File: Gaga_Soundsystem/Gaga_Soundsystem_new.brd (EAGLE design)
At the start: 160 x 100 mm, 16 parts, among them IC1 TUSB2046VF, Q2 6MHZ

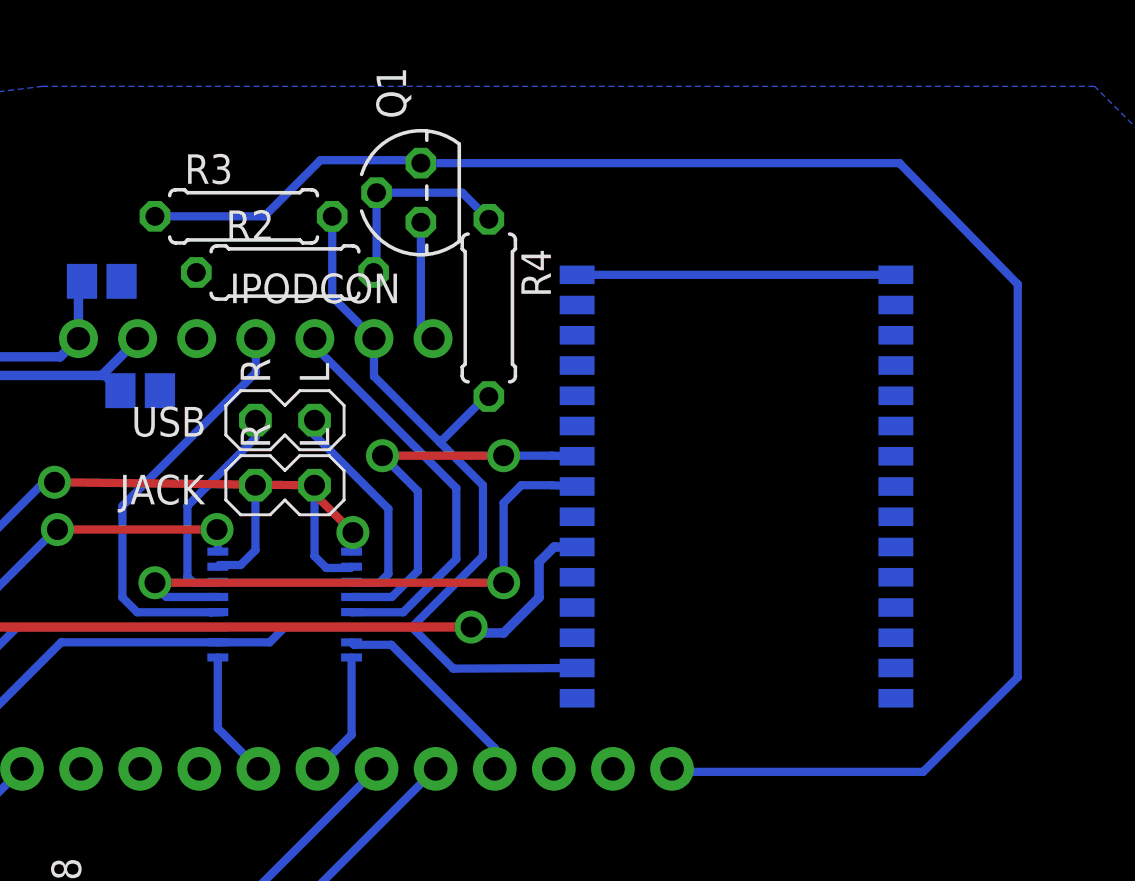
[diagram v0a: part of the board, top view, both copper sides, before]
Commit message: resistor to smd and add 3.3v
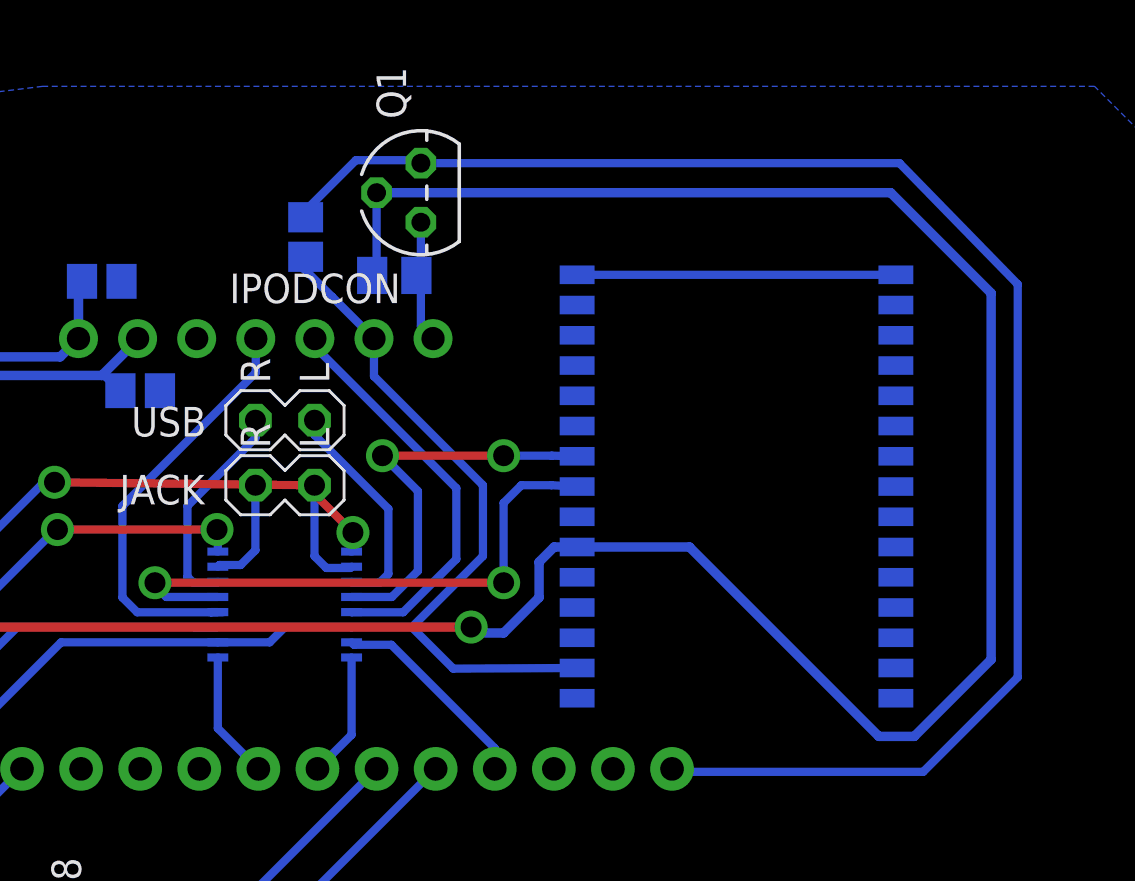
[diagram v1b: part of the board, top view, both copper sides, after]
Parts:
- removed R4: 4.7K, resistor:0207/7
- R2: device resistor:0207/7 -> resistor:M0805
- R3: device resistor:0207/7 -> resistor:R0805
- moved R2 4.70 mm to (101.1, 74.3), flipped to the bottom
- moved R3 2.81 mm to (97.3, 75.9), flipped to the bottom, turned to 270 degrees
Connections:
- removed net N$4: Q1.2, R2.2, R4.1
- net 3.3V: now also Q1.2, R2.2
- net 5.0V: no longer R4.2
- net GND: now also U$28.23, U$28.3; no longer R2.1
- net N$1: now also R2.1
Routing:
- net 3.3V: track 57.5 -> 127.7 mm
- net N$4: track 8.78 -> 0.00 mm
- net TX0: track 73.8 -> 67.9 mm
- net 5.0V: track 112.4 -> 109.0 mm
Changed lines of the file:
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@@
 <element name="U$28" library="SparkFun-Boards" package="ARDUINO_PRO_MICRO" value="ARDUINO_PRO_MICRO" x="100.33" y="45.466" rot="R270"/>
 <element name="Q1" library="transistors" package="TO-92" value="" x="102.235" y="77.851" rot="R90"/>
-<element name="R2" library="resistor" package="0207/7" value="10K" x="96.393" y="74.422"/>
-<element name="R3" library="resistor" package="0207/7" value="10K" x="94.615" y="76.835"/>
-<element name="R4" library="resistor" package="0207/7" value="4.7K" x="105.156" y="72.898" rot="R270"/>
+<element name="R2" library="resistor" package="M0805" value="10K" x="101.092" y="74.295" rot="MR0"/>
+<element name="R3" library="resistor" package="R0805" value="10K" x="97.282" y="75.946" rot="MR270"/>
 <element name="IC1" library="jt-texas" package="TQFP32-08" value="TUSB2046VF" x="78.74" y="69.596" rot="MR270"/>
 <element name="Q2" library="crystal" package="HC49/S" value="6MHZ" x="70.739" y="69.342" rot="R90">
@@
 <contactref element="Q1" pad="3"/>
 <contactref element="R3" pad="1"/>
-<wire x1="90.805" y1="76.835" x2="95.504" y2="76.835" width="0.3556" layer="16"/>
-<wire x1="95.504" y1="76.835" x2="97.917" y2="79.248" width="0.3556" layer="16"/>
-<wire x1="97.917" y1="79.248" x2="102.108" y2="79.248" width="0.3556" layer="16"/>
+<wire x1="97.028" y1="76.835" x2="97.282" y2="77.089" width="0.3556" layer="16"/>
+<wire x1="97.282" y1="77.089" x2="99.441" y2="79.248" width="0.3556" layer="16"/>
+<wire x1="99.441" y1="79.248" x2="102.108" y2="79.248" width="0.3556" layer="16"/>
 <wire x1="102.108" y1="79.248" x2="102.235" y2="79.121" width="0.3556" layer="16"/>
 <wire x1="102.235" y1="79.121" x2="122.809" y2="79.121" width="0.3556" layer="16"/>
@@
 <wire x1="123.825" y1="52.959" x2="113.157" y2="52.959" width="0.3556" layer="16"/>
 <wire x1="113.157" y1="52.959" x2="113.03" y2="53.086" width="0.3556" layer="16"/>
+<wire x1="97.282" y1="76.796" x2="97.282" y2="77.089" width="0.4064" layer="16"/>
 </signal>
 <signal name="GND">
@@
 <wire x1="93.506" y1="59.175" x2="84.881" y2="59.175" width="0.3556" layer="16"/>
 <wire x1="84.881" y1="59.175" x2="78.971" y2="53.265" width="0.3556" layer="16"/>
-<contactref element="R2" pad="1"/>
 <contactref element="IC1" pad="7"/>
 <contactref element="IC1" pad="28"/>
@@
 <wire x1="71.882" y1="65.405" x2="71.755" y2="62.865" width="0.4064" layer="16"/>
 <contactref element="IC1" pad="8"/>
+<contactref element="U$28" pad="3"/>
+<contactref element="U$28" pad="23"/>
+<wire x1="122.651" y1="56.122" x2="108.951" y2="56.122" width="0" layer="19" extent="16-16"/>
 </signal>
 <signal name="N$3">
@@
 <wire x1="101.847" y1="59.175" x2="104.902" y2="62.23" width="0.3556" layer="16"/>
 <wire x1="104.902" y1="62.23" x2="104.902" y2="65.278" width="0.3556" layer="16"/>
-<wire x1="104.902" y1="65.278" x2="103.0605" y2="67.1195" width="0.3556" layer="16"/>
-<wire x1="103.0605" y1="67.1195" x2="100.218" y2="69.962" width="0.3556" layer="16"/>
+<wire x1="104.902" y1="65.278" x2="100.218" y2="69.962" width="0.3556" layer="16"/>
 <wire x1="108.951" y1="57.422" x2="103.627" y2="57.395" width="0.3556" layer="16"/>
 <wire x1="103.627" y1="57.395" x2="101.847" y2="59.175" width="0.3556" layer="16"/>
@@
 <wire x1="76.151" y1="49.358" x2="73.914" y2="47.121" width="0.3556" layer="16"/>
 <contactref element="R3" pad="2"/>
-<contactref element="R4" pad="2"/>
-<wire x1="98.425" y1="76.835" x2="98.425" y2="73.373" width="0.3556" layer="16"/>
+<wire x1="96.735" y1="75.057" x2="97.199971875" y2="74.593678125" width="0.3556" layer="16"/>
+<wire x1="97.199971875" y1="74.593678125" x2="98.425" y2="73.373" width="0.3556" layer="16"/>
 <wire x1="98.425" y1="73.373" x2="100.218" y2="71.58" width="0.3556" layer="16"/>
-<wire x1="105.156" y1="69.088" x2="105.029" y2="69.088" width="0.3556" layer="16"/>
-<wire x1="105.029" y1="69.088" x2="103.0605" y2="67.1195" width="0.3556" layer="16"/>
+<wire x1="97.282" y1="75.096" x2="97.199971875" y2="75.096" width="0.4064" layer="16"/>
+<wire x1="97.199971875" y1="75.096" x2="97.199971875" y2="74.593678125" width="0.4064" layer="16"/>
 </signal>
 <signal name="IPODR">
@@
 <contactref element="Q1" pad="1"/>
 <contactref element="U$5" pad="P$5"/>
-<wire x1="102.235" y1="76.581" x2="102.235" y2="72.103" width="0.3556" layer="16"/>
+<wire x1="102.235" y1="76.581" x2="102.235" y2="74.422" width="0.3556" layer="16"/>
+<wire x1="102.235" y1="74.422" x2="102.235" y2="72.103" width="0.3556" layer="16"/>
 <wire x1="102.235" y1="72.103" x2="102.758" y2="71.58" width="0.3556" layer="16"/>
-</signal>
-<signal name="N$4">
-<contactref element="Q1" pad="2"/>
-<contactref element="R2" pad="2"/>
-<contactref element="R4" pad="1"/>
-<wire x1="100.33" y1="77.851" x2="104.013" y2="77.851" width="0.3556" layer="16"/>
-<wire x1="104.013" y1="77.851" x2="105.156" y2="76.708" width="0.3556" layer="16"/>
-<wire x1="100.33" y1="77.851" x2="100.33" y2="74.549" width="0.3556" layer="16"/>
-<wire x1="100.33" y1="74.549" x2="100.203" y2="74.422" width="0.3556" layer="16"/>
+<contactref element="R2" pad="1"/>
+<wire x1="102.042" y1="74.295" x2="102.235" y2="74.295" width="0.4064" layer="16"/>
+<wire x1="102.235" y1="74.295" x2="102.235" y2="74.422" width="0.4064" layer="16"/>
 </signal>
 <signal name="N$2">
@@
 <wire x1="79.94" y1="73.8886" x2="79.94" y2="72.701" width="0.4064" layer="16"/>
 <wire x1="79.94" y1="72.701" x2="77.47" y2="70.231" width="0.4064" layer="16"/>
+<contactref element="Q1" pad="2"/>
+<contactref element="R2" pad="2"/>
+<wire x1="100.33" y1="77.851" x2="100.33" y2="74.549" width="0.3556" layer="16"/>
+<wire x1="100.142" y1="74.295" x2="100.33" y2="74.295" width="0.4064" layer="16"/>
+<wire x1="100.33" y1="74.295" x2="100.33" y2="74.549" width="0.4064" layer="16"/>
+<wire x1="108.951" y1="62.622" x2="113.781" y2="62.622" width="0.4064" layer="16"/>
+<wire x1="113.781" y1="62.622" x2="121.92" y2="54.483" width="0.4064" layer="16"/>
+<wire x1="121.92" y1="54.483" x2="123.444" y2="54.483" width="0.4064" layer="16"/>
+<wire x1="123.444" y1="54.483" x2="126.746" y2="57.785" width="0.4064" layer="16"/>
+<wire x1="126.746" y1="57.785" x2="126.746" y2="73.533" width="0.4064" layer="16"/>
+<wire x1="126.746" y1="73.533" x2="122.428" y2="77.851" width="0.4064" layer="16"/>
+<wire x1="122.428" y1="77.851" x2="100.33" y2="77.851" width="0.4064" layer="16"/>
 </signal>
 </signals>
